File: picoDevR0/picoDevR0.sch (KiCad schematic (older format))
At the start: 3 parts, among them J1 Conn_01x20_Female, J2 Conn_01x20_Female, U1 Pico

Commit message: added library
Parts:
- J1, J2: footprint Connector_PinSocket_2.54mm:PinSocket_1x20_P2.54mm_Horizontal -> Connector_PinSocket_2.54mm:PinSocket_1x20_P2.54mm_Vertical
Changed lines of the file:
@@
 F 0 "J2" H 3042 5735 50  0000 C CNN
 F 1 "Conn_01x20_Female" H 3042 5644 50  0000 C CNN
-F 2 "Connector_PinSocket_2.54mm:PinSocket_1x20_P2.54mm_Horizontal" H 3150 4650 50  0001 C CNN
+F 2 "Connector_PinSocket_2.54mm:PinSocket_1x20_P2.54mm_Vertical" H 3150 4650 50  0001 C CNN
 F 3 "~" H 3150 4650 50  0001 C CNN
 	1    3150 4650
@@
 F 0 "J1" H 5728 4626 50  0000 L CNN
 F 1 "Conn_01x20_Female" H 5728 4535 50  0000 L CNN
-F 2 "Connector_PinSocket_2.54mm:PinSocket_1x20_P2.54mm_Horizontal" H 5700 4650 50  0001 C CNN
+F 2 "Connector_PinSocket_2.54mm:PinSocket_1x20_P2.54mm_Vertical" H 5700 4650 50  0001 C CNN
 F 3 "~" H 5700 4650 50  0001 C CNN
 	1    5700 4650

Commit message: added barrel, have to fix switch and add connections
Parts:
- removed U1: Pico, rp2040footer:RPi_Pico_SMD_TH, symbol rp2040:Pico
- added 12Vout1: Conn_01x04_Male, Connector_PinHeader_1.00mm:PinHeader_1x04_P1.00mm_Vertical, symbol Connector:Conn_01x04_Male
- added J1: Jack-DC, Connector_BarrelJack:BarrelJack_CUI_PJ-063AH_Horizontal, symbol Connector:Jack-DC
- added Main_SW1: SW_MEC_5G_LED, LED_THT:LED_D3.0mm, symbol Switch:SW_MEC_5G_LED
- added RP2040Board1: Pico, picoFootPrint:RPi_Pico_SMD_TH, symbol picoLibRP2040:Pico
- added U1: LM1117-3.3, Connector_PinHeader_1.00mm:PinHeader_1x03_P1.00mm_Vertical, symbol Regulator_Linear:LM1117-3.3
- J2: value Conn_01x20_Female -> Pico1to20
- renumbered J1 to pico21to40
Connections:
- wire segments 10 -> 26
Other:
- moved on the sheet: pico21to40
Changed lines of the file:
@@
 $EndDescr
-$Comp
-L rp2040:Pico U1
-U 1 1 606E76B4
-P 4700 4700
-F 0 "U1" H 4700 5915 50  0000 C CNN
-F 1 "Pico" H 4700 5824 50  0000 C CNN
-F 2 "rp2040footer:RPi_Pico_SMD_TH" V 4700 4700 50  0001 C CNN
-F 3 "" H 4700 4700 50  0001 C CNN
-	1    4700 4700
-	1    0    0    -1
-$EndComp
-Wire Wire Line
-	5400 3750 5500 3750
-Wire Wire Line
-	5400 3850 5500 3850
-Wire Wire Line
-	5500 3950 5400 3950
-Wire Wire Line
-	5400 5650 5500 5650
 $Comp
 L Connector:Conn_01x20_Female J2
@@
 P 3150 4650
 F 0 "J2" H 3042 5735 50  0000 C CNN
-F 1 "Conn_01x20_Female" H 3042 5644 50  0000 C CNN
+F 1 "Pico1to20" H 3042 5644 50  0000 C CNN
 F 2 "Connector_PinSocket_2.54mm:PinSocket_1x20_P2.54mm_Vertical" H 3150 4650 50  0001 C CNN
 F 3 "~" H 3150 4650 50  0001 C CNN
@@
 	3350 5650 4000 5650
 $Comp
-L Connector:Conn_01x20_Female J1
+L Connector:Conn_01x20_Female pico21to40
 U 1 1 606EDD3B
-P 5700 4650
-F 0 "J1" H 5728 4626 50  0000 L CNN
-F 1 "Conn_01x20_Female" H 5728 4535 50  0000 L CNN
-F 2 "Connector_PinSocket_2.54mm:PinSocket_1x20_P2.54mm_Vertical" H 5700 4650 50  0001 C CNN
-F 3 "~" H 5700 4650 50  0001 C CNN
-	1    5700 4650
+P 6450 4650
+F 0 "pico21to40" H 6478 4626 50  0000 L CNN
+F 1 "Conn_01x20_Female" H 6478 4535 50  0000 L CNN
+F 2 "Connector_PinSocket_2.54mm:PinSocket_1x20_P2.54mm_Vertical" H 6450 4650 50  0001 C CNN
+F 3 "~" H 6450 4650 50  0001 C CNN
+	1    6450 4650
 	1    0    0    -1
 $EndComp
+Wire Wire Line
+	4000 4250 3350 4250
+Wire Wire Line
+	5400 3750 6250 3750
+Wire Wire Line
+	5400 3950 6250 3950
+$Comp
+L picoLibRP2040:Pico RP2040Board1
+U 1 1 60A03192
+P 4700 4700
+F 0 "RP2040Board1" H 4700 5915 50  0000 C CNN
+F 1 "Pico" H 4700 5824 50  0000 C CNN
+F 2 "picoFootPrint:RPi_Pico_SMD_TH" V 4700 4700 50  0001 C CNN
+F 3 "" H 4700 4700 50  0001 C CNN
+	1    4700 4700
+	1    0    0    -1
+$EndComp
+Wire Wire Line
+	5400 5650 6250 5650
+$Comp
+L Connector:Jack-DC J1
+U 1 1 60A0CA80
+P 6150 2300
+F 0 "J1" H 5920 2350 50  0000 R CNN
+F 1 "Jack-DC" H 5920 2259 50  0000 R CNN
+F 2 "Connector_BarrelJack:BarrelJack_CUI_PJ-063AH_Horizontal" H 6200 2260 50  0001 C CNN
+F 3 "~" H 6200 2260 50  0001 C CNN
+	1    6150 2300
+	-1   0    0    -1
+$EndComp
+$Comp
+L Regulator_Linear:LM1117-3.3 U1
+U 1 1 60A164B8
+P 4800 2200
+F 0 "U1" H 4800 2442 50  0000 C CNN
+F 1 "LM1117-3.3" H 4800 2351 50  0000 C CNN
+F 2 "Connector_PinHeader_1.00mm:PinHeader_1x03_P1.00mm_Vertical" H 4800 2200 50  0001 C CNN
+F 3 "http://www.ti.com/lit/ds/symlink/lm1117.pdf" H 4800 2200 50  0001 C CNN
+	1    4800 2200
+	-1   0    0    -1
+$EndComp
+Wire Wire Line
+	5850 2400 5850 2500
+$Comp
+L Connector:Conn_01x04_Male 12Vout1
+U 1 1 60A2414E
+P 6250 2900
+F 0 "12Vout1" H 6358 3181 50  0000 C CNN
+F 1 "Conn_01x04_Male" H 6358 3090 50  0000 C CNN
+F 2 "Connector_PinHeader_1.00mm:PinHeader_1x04_P1.00mm_Vertical" H 6250 2900 50  0001 C CNN
+F 3 "~" H 6250 2900 50  0001 C CNN
+	1    6250 2900
+	1    0    0    -1
+$EndComp
+Wire Wire Line
+	6450 2800 6450 2900
+Wire Wire Line
+	6450 3000 6450 2900
+Connection ~ 6450 2900
+Wire Wire Line
+	6450 3000 6450 3100
+Connection ~ 6450 3000
+Connection ~ 6450 3100
+Wire Wire Line
+	6450 3100 6450 3150
+Connection ~ 6450 2800
+Wire Wire Line
+	6450 2800 6450 2200
+Wire Wire Line
+	4500 2200 4500 3850
+Connection ~ 5400 3850
+Wire Wire Line
+	5400 3850 6250 3850
+Wire Wire Line
+	4800 2500 4800 3950
+Connection ~ 4800 2500
+Connection ~ 5400 3950
+$Comp
+L Switch:SW_MEC_5G_LED Main_SW1
+U 1 1 60A518BE
+P 5450 2300
+F 0 "Main_SW1" H 5450 2685 50  0000 C CNN
+F 1 "SW_MEC_5G_LED" H 5450 2594 50  0000 C CNN
+F 2 "LED_THT:LED_D3.0mm" H 5450 2600 50  0001 C CNN
+F 3 "http://www.apem.com/int/index.php?controller=attachment&id_attachment=488" H 5450 2600 50  0001 C CNN
+	1    5450 2300
+	1    0    0    -1
+$EndComp
+Wire Wire Line
+	5650 2200 5850 2200
+Connection ~ 5850 2200
+Wire Wire Line
+	5850 2200 6450 2200
+Wire Wire Line
+	5250 2200 5100 2200
+Wire Wire Line
+	4800 2500 5850 2500
+Connection ~ 5300 3950
+Wire Wire Line
+	5300 3950 5400 3950
+Wire Wire Line
+	4500 3850 5400 3850
+Wire Wire Line
+	4800 3950 5400 3950
 $EndSCHEMATC

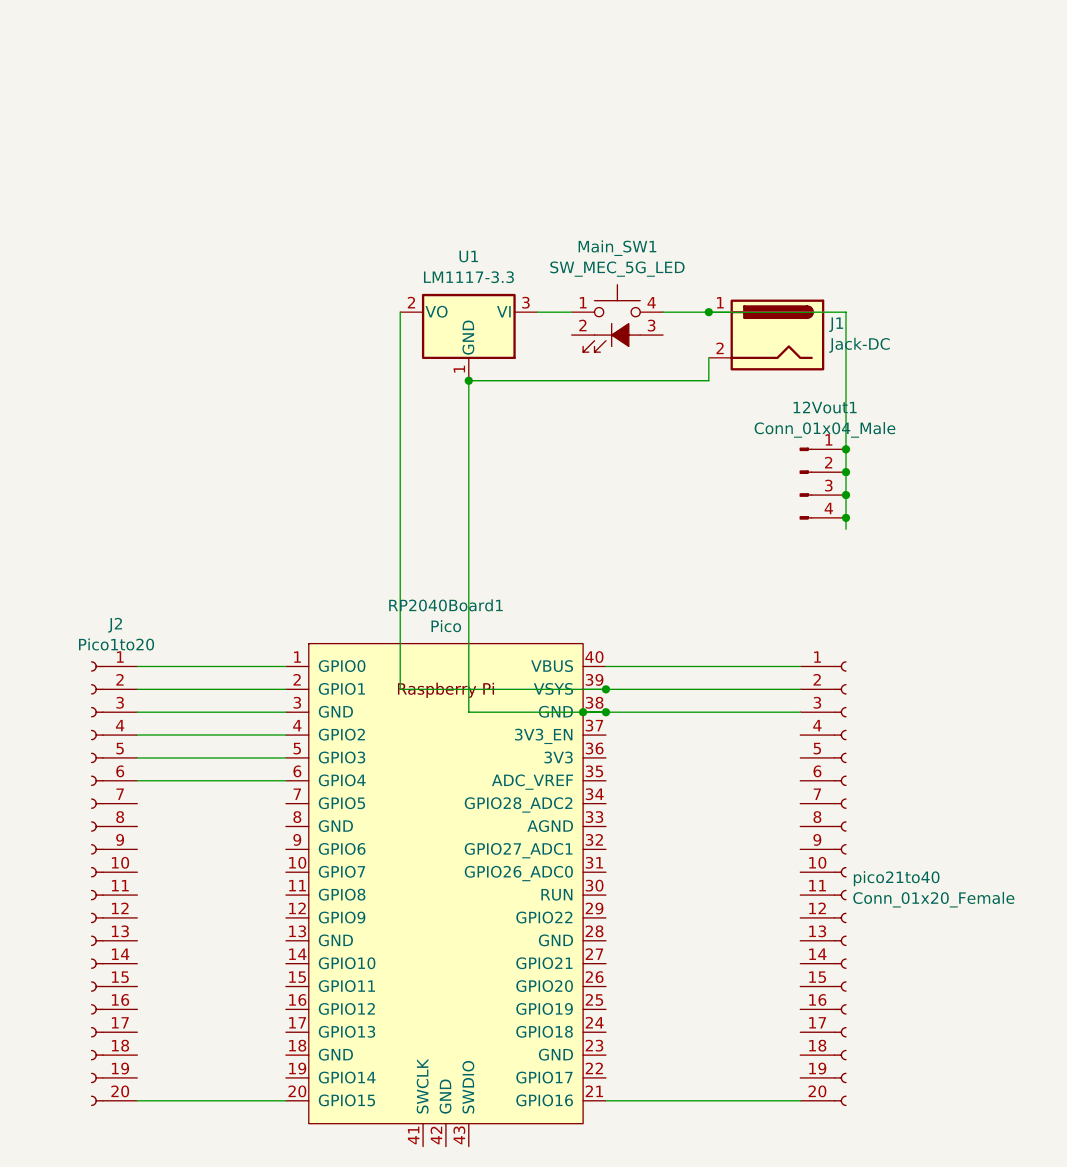
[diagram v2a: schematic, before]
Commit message: added one-one pin connections in sch
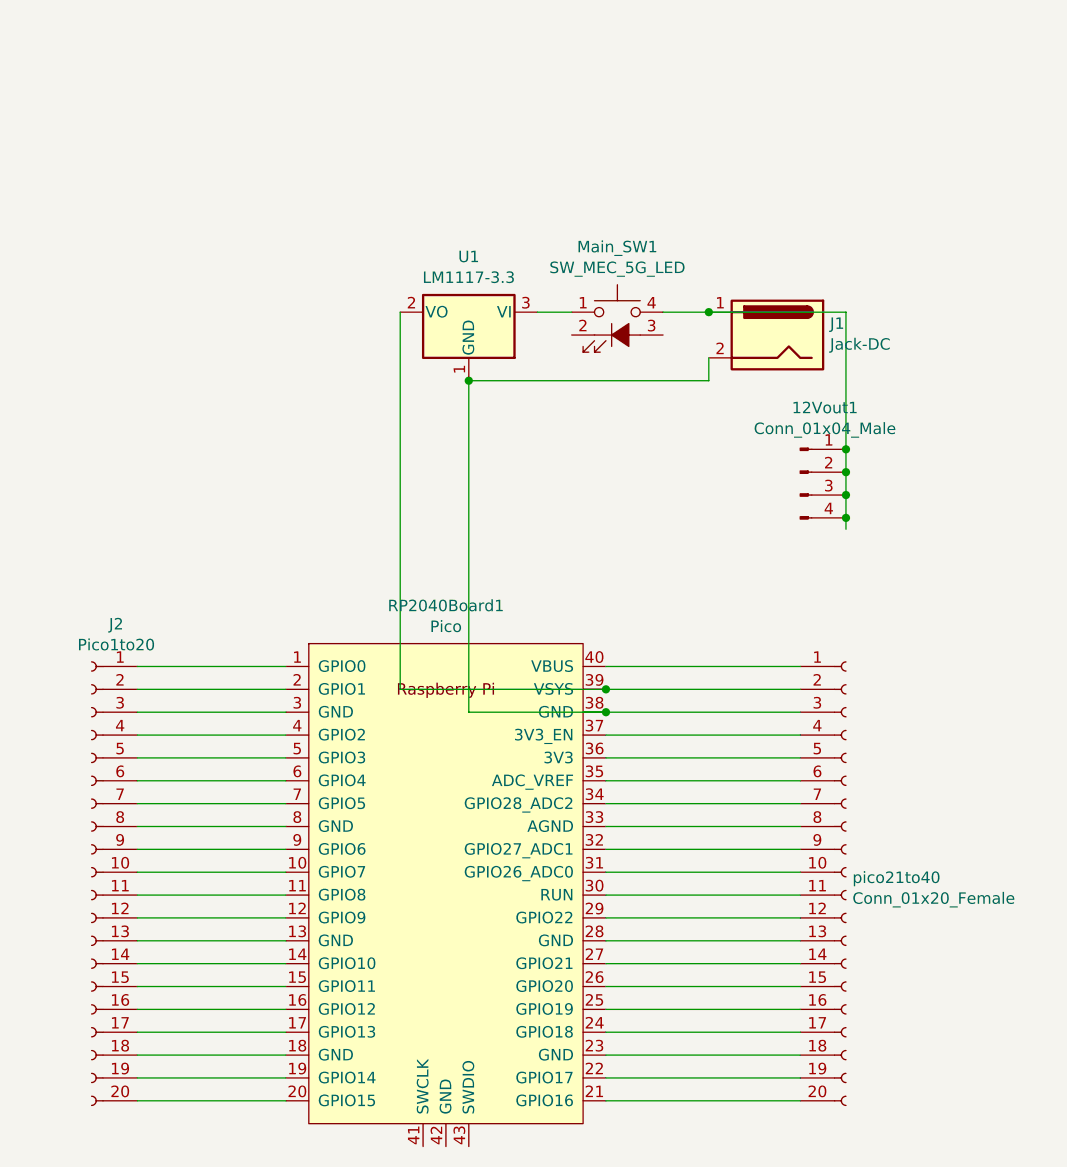
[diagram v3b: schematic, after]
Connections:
- wire segments 26 -> 55
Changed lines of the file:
@@
 Wire Wire Line
 	4800 2500 5850 2500
-Connection ~ 5300 3950
+Wire Wire Line
+	4500 3850 5400 3850
+Wire Wire Line
+	5400 4050 6250 4050
 Wire Wire Line
 	5300 3950 5400 3950
 Wire Wire Line
-	4500 3850 5400 3850
+	4800 3950 5400 3950
 Wire Wire Line
-	4800 3950 5400 3950
+	5400 4150 6250 4150
+Wire Wire Line
+	6250 4250 5400 4250
+Wire Wire Line
+	6250 4350 5400 4350
+Wire Wire Line
+	5400 4450 6250 4450
+Wire Wire Line
+	6250 4550 5400 4550
+Wire Wire Line
+	6250 4650 5400 4650
+Wire Wire Line
+	6250 4750 5400 4750
+Wire Wire Line
+	6250 4850 5400 4850
+Wire Wire Line
+	5400 4950 6250 4950
+Wire Wire Line
+	6250 5050 5400 5050
+Wire Wire Line
+	5400 5150 6250 5150
+Wire Wire Line
+	5400 5250 6250 5250
+Wire Wire Line
+	5400 5350 6250 5350
+Wire Wire Line
+	5400 5450 6250 5450
+Wire Wire Line
+	6250 5550 5400 5550
+Wire Wire Line
+	4000 4350 3350 4350
+Wire Wire Line
+	4000 4450 3350 4450
+Wire Wire Line
+	4000 4550 3350 4550
+Wire Wire Line
+	4000 4650 3350 4650
+Wire Wire Line
+	3350 4750 4000 4750
+Wire Wire Line
+	3350 4850 4000 4850
+Wire Wire Line
+	4000 4950 3350 4950
+Wire Wire Line
+	3350 5050 4000 5050
+Wire Wire Line
+	4000 5150 3350 5150
+Wire Wire Line
+	3350 5250 4000 5250
+Wire Wire Line
+	4000 5350 3350 5350
+Wire Wire Line
+	3350 5450 4000 5450
+Wire Wire Line
+	4000 5550 3350 5550
 $EndSCHEMATC

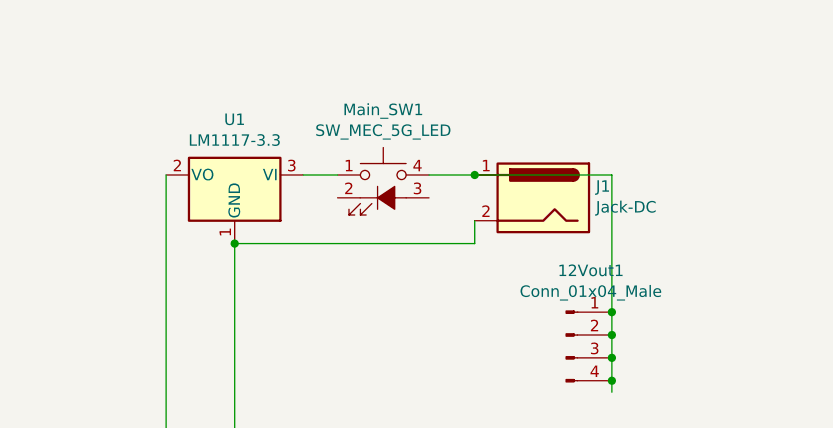
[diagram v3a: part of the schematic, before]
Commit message: replaced switch and LED
replaced earlier component with 2 seperate one's for ease of footprint assigning
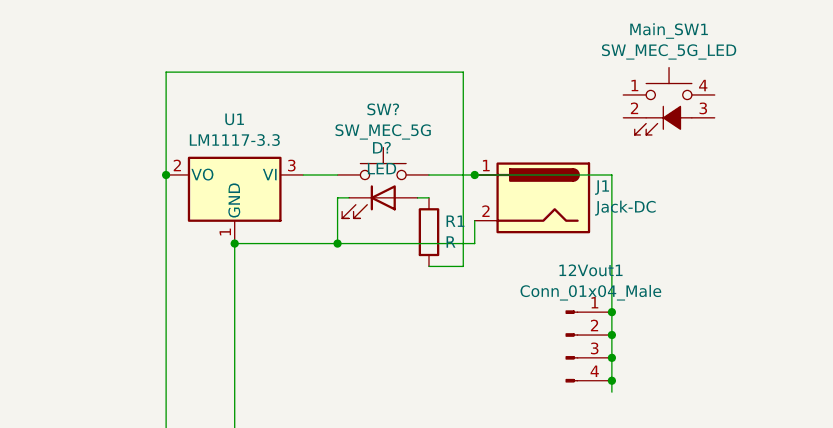
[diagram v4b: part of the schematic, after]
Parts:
- added D?: LED, symbol Device:LED
- added R1: R, Resistor_THT:R_Axial_DIN0922_L20.0mm_D9.0mm_P30.48mm_Horizontal, symbol Device:R
- added SW?: SW_MEC_5G, symbol Switch:SW_MEC_5G
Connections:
- wire segments 55 -> 63
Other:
- moved on the sheet: Main_SW1
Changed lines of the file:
@@
 L Switch:SW_MEC_5G_LED Main_SW1
 U 1 1 60A518BE
-P 5450 2300
-F 0 "Main_SW1" H 5450 2685 50  0000 C CNN
-F 1 "SW_MEC_5G_LED" H 5450 2594 50  0000 C CNN
-F 2 "LED_THT:LED_D3.0mm" H 5450 2600 50  0001 C CNN
-F 3 "http://www.apem.com/int/index.php?controller=attachment&id_attachment=488" H 5450 2600 50  0001 C CNN
-	1    5450 2300
+P 6700 1950
+F 0 "Main_SW1" H 6700 2335 50  0000 C CNN
+F 1 "SW_MEC_5G_LED" H 6700 2244 50  0000 C CNN
+F 2 "LED_THT:LED_D3.0mm" H 6700 2250 50  0001 C CNN
+F 3 "http://www.apem.com/int/index.php?controller=attachment&id_attachment=488" H 6700 2250 50  0001 C CNN
+	1    6700 1950
 	1    0    0    -1
 $EndComp
@@
 	5850 2200 6450 2200
 Wire Wire Line
-	5250 2200 5100 2200
-Wire Wire Line
-	4800 2500 5850 2500
+	4800 2500 5250 2500
 Wire Wire Line
 	4500 3850 5400 3850
@@
 Wire Wire Line
 	4000 5550 3350 5550
+$Comp
+L Device:R R1
+U 1 1 609F8EDD
+P 5650 2450
+F 0 "R1" H 5720 2496 50  0000 L CNN
+F 1 "R" H 5720 2405 50  0000 L CNN
+F 2 "Resistor_THT:R_Axial_DIN0922_L20.0mm_D9.0mm_P30.48mm_Horizontal" V 5580 2450 50  0001 C CNN
+F 3 "~" H 5650 2450 50  0001 C CNN
+	1    5650 2450
+	1    0    0    -1
+$EndComp
+Wire Wire Line
+	5650 2600 5800 2600
+Wire Wire Line
+	5800 2600 5800 1750
+Wire Wire Line
+	5250 2300 5250 2500
+Connection ~ 5250 2500
+Wire Wire Line
+	5250 2500 5850 2500
+Wire Wire Line
+	5100 2200 5250 2200
+Wire Wire Line
+	4500 1750 4500 2200
+Wire Wire Line
+	4500 1750 5800 1750
+Connection ~ 4500 2200
+$Comp
+L Switch:SW_MEC_5G SW?
+U 1 1 60A09B24
+P 5450 2200
+F 0 "SW?" H 5450 2485 50  0000 C CNN
+F 1 "SW_MEC_5G" H 5450 2394 50  0000 C CNN
+F 2 "" H 5450 2400 50  0001 C CNN
+F 3 "http://www.apem.com/int/index.php?controller=attachment&id_attachment=488" H 5450 2400 50  0001 C CNN
+	1    5450 2200
+	1    0    0    -1
+$EndComp
+$Comp
+L Device:LED D?
+U 1 1 60A0A221
+P 5450 2300
+F 0 "D?" H 5443 2517 50  0000 C CNN
+F 1 "LED" H 5443 2426 50  0000 C CNN
+F 2 "" H 5450 2300 50  0001 C CNN
+F 3 "~" H 5450 2300 50  0001 C CNN
+	1    5450 2300
+	1    0    0    -1
+$EndComp
+Wire Wire Line
+	5250 2300 5300 2300
+Wire Wire Line
+	5650 2300 5600 2300
 $EndSCHEMATC

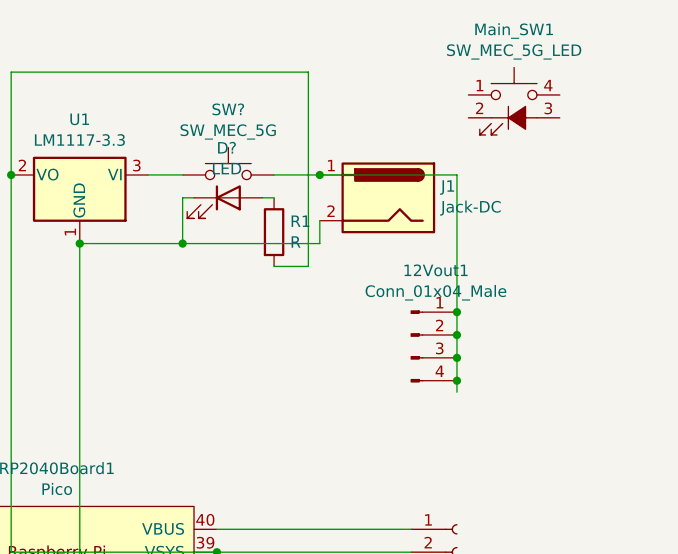
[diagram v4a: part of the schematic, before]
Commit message: LM footprint changed to female
also there seems to be an issue with the button footprint, need one proper 2-hole button
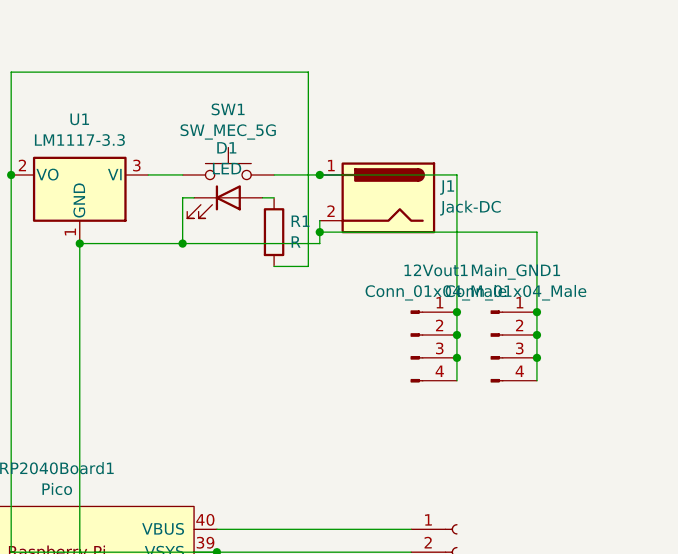
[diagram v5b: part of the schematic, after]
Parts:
- removed Main_SW1: SW_MEC_5G_LED, LED_THT:LED_D3.0mm, symbol Switch:SW_MEC_5G_LED
- added Main_GND1: Conn_01x04_Male, Connector_PinHeader_1.00mm:PinHeader_1x04_P1.00mm_Vertical, symbol Connector:Conn_01x04_Male
- D1: renamed from D?; footprint (none) -> LED_THT:LED_D10.0mm
- SW1: renamed from SW?; footprint (none) -> Button_Switch_THT:SW_CW_GPTS203211B
- U1: footprint Connector_PinHeader_1.00mm:PinHeader_1x03_P1.00mm_Vertical -> Connector_PinSocket_1.00mm:PinSocket_1x03_P1.00mm_Vertical
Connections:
- net at D1.1 (K), J1.2, RP2040Board1.38 (GND)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: now also Main_GND1.1 (Pin_1), Main_GND1.2 (Pin_2), Main_GND1.3 (Pin_3), Main_GND1.4 (Pin_4)
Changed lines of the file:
@@
 F 0 "U1" H 4800 2442 50  0000 C CNN
 F 1 "LM1117-3.3" H 4800 2351 50  0000 C CNN
-F 2 "Connector_PinHeader_1.00mm:PinHeader_1x03_P1.00mm_Vertical" H 4800 2200 50  0001 C CNN
+F 2 "Connector_PinSocket_1.00mm:PinSocket_1x03_P1.00mm_Vertical" H 4800 2200 50  0001 C CNN
 F 3 "http://www.ti.com/lit/ds/symlink/lm1117.pdf" H 4800 2200 50  0001 C CNN
 	1    4800 2200
@@
 $EndComp
 Wire Wire Line
-	5850 2400 5850 2500
+	5850 2400 5850 2450
 $Comp
 L Connector:Conn_01x04_Male 12Vout1
@@
 $EndComp
 Wire Wire Line
-	6450 2800 6450 2900
-Wire Wire Line
-	6450 3000 6450 2900
-Connection ~ 6450 2900
-Wire Wire Line
-	6450 3000 6450 3100
-Connection ~ 6450 3000
-Connection ~ 6450 3100
-Wire Wire Line
-	6450 3100 6450 3150
-Connection ~ 6450 2800
-Wire Wire Line
-	6450 2800 6450 2200
-Wire Wire Line
 	4500 2200 4500 3850
 Connection ~ 5400 3850
@@
 Connection ~ 4800 2500
 Connection ~ 5400 3950
-$Comp
-L Switch:SW_MEC_5G_LED Main_SW1
-U 1 1 60A518BE
-P 6700 1950
-F 0 "Main_SW1" H 6700 2335 50  0000 C CNN
-F 1 "SW_MEC_5G_LED" H 6700 2244 50  0000 C CNN
-F 2 "LED_THT:LED_D3.0mm" H 6700 2250 50  0001 C CNN
-F 3 "http://www.apem.com/int/index.php?controller=attachment&id_attachment=488" H 6700 2250 50  0001 C CNN
-	1    6700 1950
-	1    0    0    -1
-$EndComp
 Wire Wire Line
 	5650 2200 5850 2200
@@
 Connection ~ 4500 2200
 $Comp
-L Switch:SW_MEC_5G SW?
+L Switch:SW_MEC_5G SW1
 U 1 1 60A09B24
 P 5450 2200
-F 0 "SW?" H 5450 2485 50  0000 C CNN
+F 0 "SW1" H 5450 2485 50  0000 C CNN
 F 1 "SW_MEC_5G" H 5450 2394 50  0000 C CNN
-F 2 "" H 5450 2400 50  0001 C CNN
+F 2 "Button_Switch_THT:SW_CW_GPTS203211B" H 5450 2400 50  0001 C CNN
 F 3 "http://www.apem.com/int/index.php?controller=attachment&id_attachment=488" H 5450 2400 50  0001 C CNN
 	1    5450 2200
@@
 $EndComp
 $Comp
-L Device:LED D?
+L Device:LED D1
 U 1 1 60A0A221
 P 5450 2300
-F 0 "D?" H 5443 2517 50  0000 C CNN
+F 0 "D1" H 5443 2517 50  0000 C CNN
 F 1 "LED" H 5443 2426 50  0000 C CNN
-F 2 "" H 5450 2300 50  0001 C CNN
+F 2 "LED_THT:LED_D10.0mm" H 5450 2300 50  0001 C CNN
 F 3 "~" H 5450 2300 50  0001 C CNN
 	1    5450 2300
@@
 Wire Wire Line
 	5650 2300 5600 2300
+$Comp
+L Connector:Conn_01x04_Male Main_GND1
+U 1 1 60A16EFC
+P 6600 2900
+F 0 "Main_GND1" H 6708 3181 50  0000 C CNN
+F 1 "Conn_01x04_Male" H 6708 3090 50  0000 C CNN
+F 2 "Connector_PinHeader_1.00mm:PinHeader_1x04_P1.00mm_Vertical" H 6600 2900 50  0001 C CNN
+F 3 "~" H 6600 2900 50  0001 C CNN
+	1    6600 2900
+	1    0    0    -1
+$EndComp
+Wire Wire Line
+	6800 2800 6800 2450
+Wire Wire Line
+	6800 2450 5850 2450
+Connection ~ 5850 2450
+Wire Wire Line
+	5850 2450 5850 2500
+Wire Wire Line
+	6800 2900 6800 2800
+Connection ~ 6800 2900
+Wire Wire Line
+	6800 2900 6800 3000
+Connection ~ 6800 2800
+Wire Wire Line
+	6800 3100 6800 3000
+Connection ~ 6800 3000
+Connection ~ 6450 2800
+Wire Wire Line
+	6450 2200 6450 2800
+Wire Wire Line
+	6450 2800 6450 2900
+Wire Wire Line
+	6450 3100 6450 3000
+Connection ~ 6450 2900
+Connection ~ 6450 3000
+Wire Wire Line
+	6450 3000 6450 2900
 $EndSCHEMATC
